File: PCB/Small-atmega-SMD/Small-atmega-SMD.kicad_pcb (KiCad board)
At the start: 2 copper layers, 65.1 x 96.9 mm, 31 parts, among them J1 Daisy port out, J2 ICSP_ISP6, J3 UART, J4 Daisy port in, K1 HYC77-TF09-200, U1 PC817C-S, U2 ATmega328P-AU, U3 SE5218, U4 TXB0104PWR, Y1 Resonator_GND2

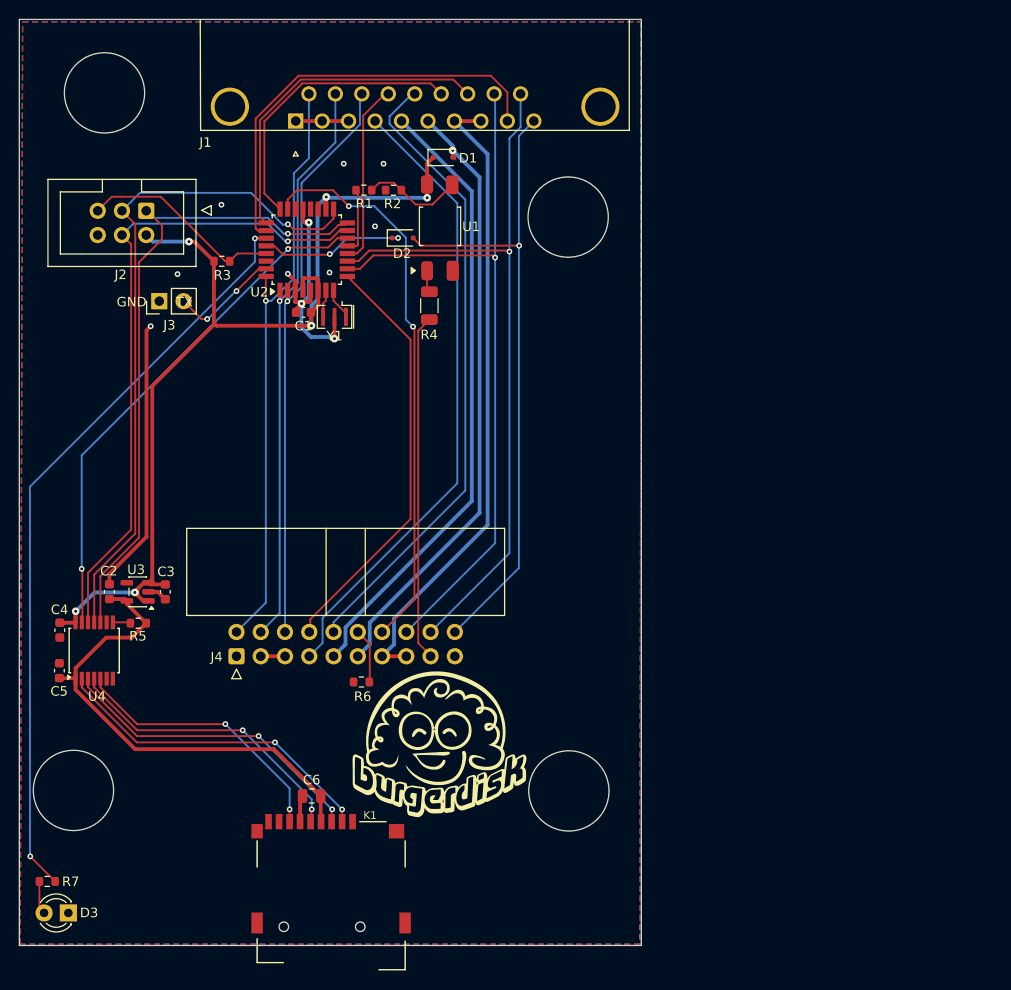
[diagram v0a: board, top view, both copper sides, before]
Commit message: Add SD module header, for hackers
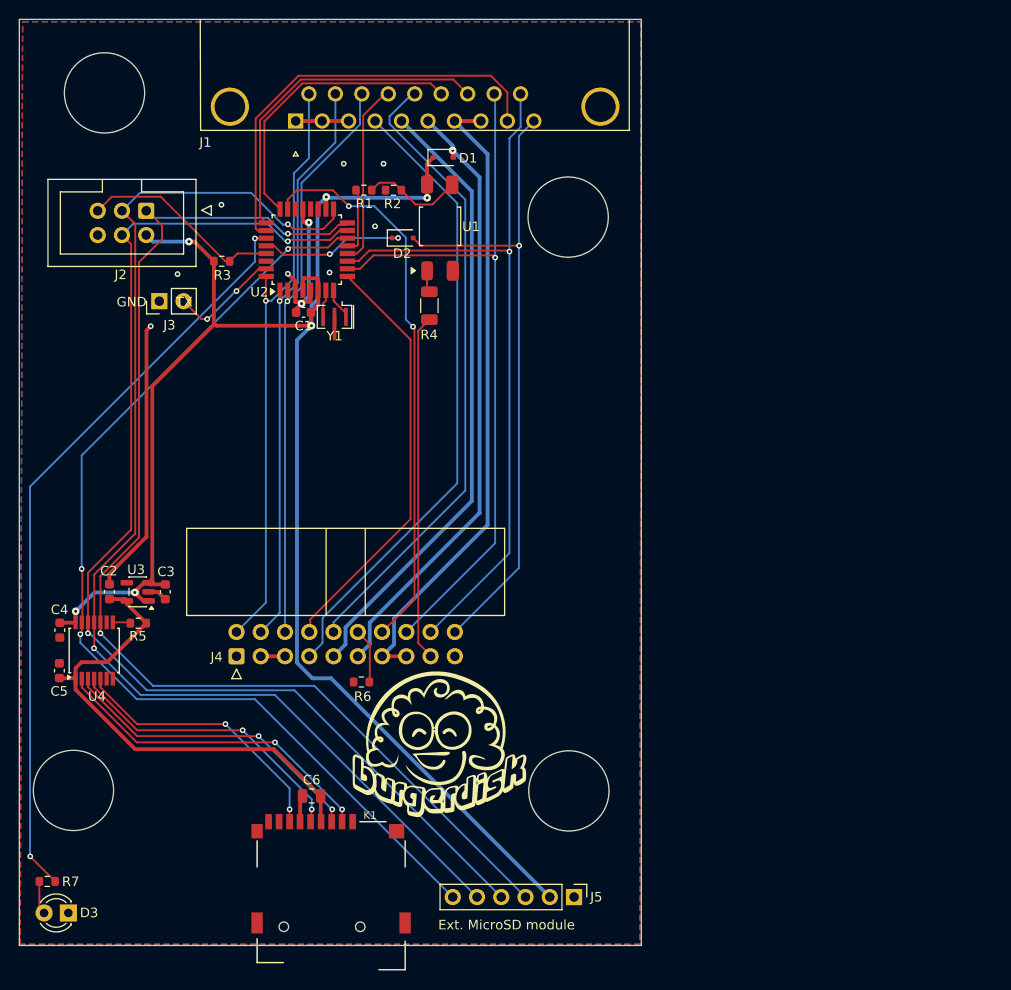
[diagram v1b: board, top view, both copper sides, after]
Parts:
- added J5: Ext. MicroSD module, Connector_PinHeader_2.54mm:PinHeader_1x06_P2.54mm_Vertical, F.Cu at (157.6, 135.2)
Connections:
- D3 pad 2: Net-(D3-A) -> LED
- R7 pad 1: Net-(D3-A) -> LED
- R7 pad 2: LED -> Net-(U2-PC4)
- U2 pad 27: LED -> Net-(U2-PC4)
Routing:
- net Net-(U2-PC4): track 0.00 -> 79.3 mm, vias 0 -> 2
- net LED: track 79.3 -> 2.81 mm, vias 2 -> 0
- net 5V_burgerDisk: track 109.5 -> 182.0 mm
- net MISO: track 68.9 -> 126.0 mm, vias 1 -> 2
- net MOSI: track 68.2 -> 124.1 mm, vias 1 -> 2
- net SCK: track 71.4 -> 125.0 mm, vias 1 -> 2
- net CS: track 54.7 -> 106.9 mm, vias 2 -> 3
- net GND: track 69.1 -> 62.7 mm, vias 11 -> 10
- net Net-(D3-A): track 2.81 -> 0.00 mm

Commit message: Add solder pads for hacking
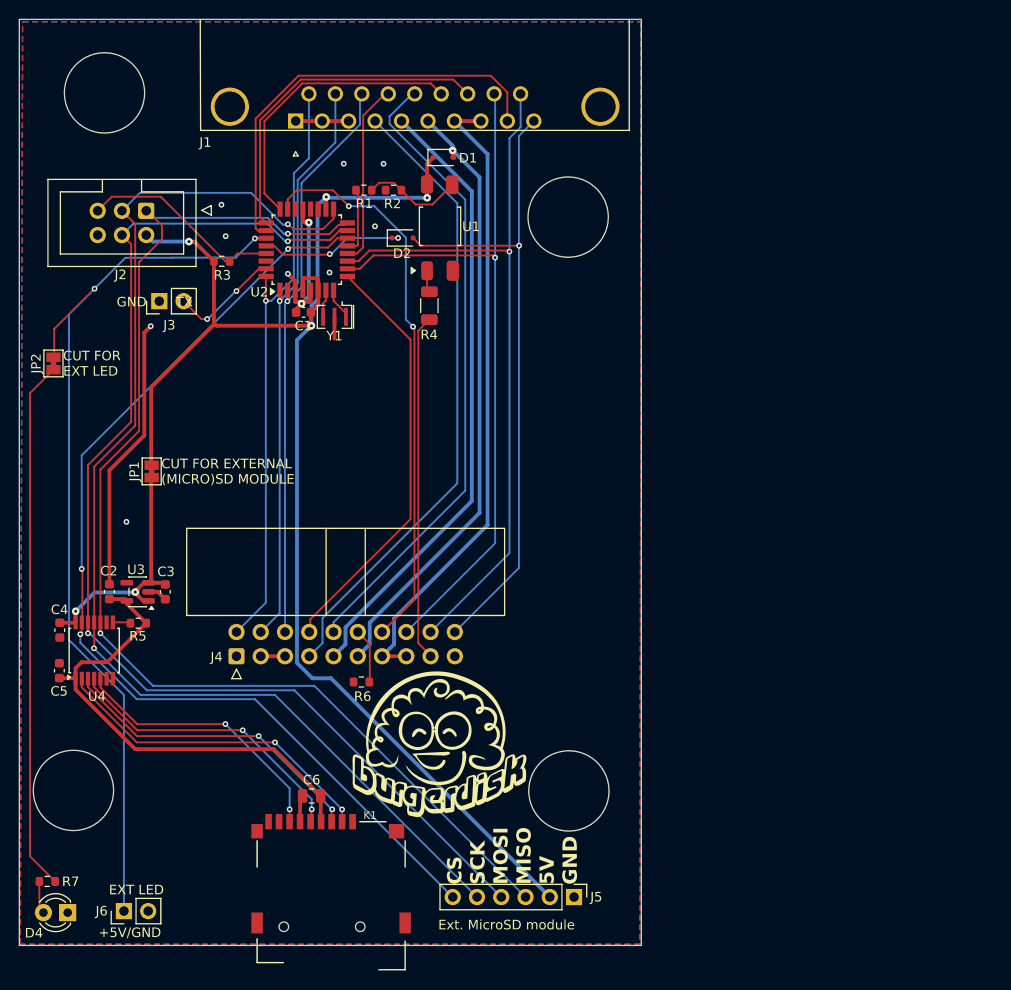
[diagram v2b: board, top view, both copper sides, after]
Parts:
- removed D3: LED, LED_THT:LED_D3.0mm
- added D4: LED, LED_THT:LED_D3.0mm, F.Cu at (104.6, 136.8)
- added J6: EXT LED, Connector_PinHeader_2.54mm:PinHeader_1x02_P2.54mm_Vertical, F.Cu at (110.5, 136.7)
- added JP1: INT MICROSD JUMPER, Jumper:SolderJumper-2_P1.3mm_Bridged_Pad1.0x1.5mm, F.Cu at (113.4, 90.6)
- added JP2: INT/EXT LED JUMPER, Jumper:SolderJumper-2_P1.3mm_Bridged_Pad1.0x1.5mm, F.Cu at (103.1, 79.3)
- C1: value 100nF -> 100n
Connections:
- C3 pad 2: 5V_burgerDisk -> 5V_intMicroSD
- C4 pad 2: 5V_burgerDisk -> 5V_intMicroSD
- R7 pad 1: LED -> Net-(D4-A)
- R7 pad 2: Net-(U2-PC4) -> Net-(JP2-A)
- U2 pad 27: Net-(U2-PC4) -> LED
- U3 pad 1: 5V_burgerDisk -> 5V_intMicroSD
- U3 pad 3: 5V_burgerDisk -> 5V_intMicroSD
- U4 pad 14: 5V_burgerDisk -> 5V_intMicroSD
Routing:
- net LED: track 2.81 -> 98.0 mm, vias 0 -> 2
- net Net-(U2-PC4): track 79.3 -> 0.00 mm, vias 2 -> 0
- net Net-(JP2-A): track 0.00 -> 55.7 mm
- net 5V_burgerDisk: track 182.0 -> 153.6 mm, vias 6 -> 4
- net 5V_intMicroSD: track 0.00 -> 27.2 mm, vias 0 -> 2
- net Net-(D4-A): track 0.00 -> 3.44 mm
- net GND: vias 10 -> 11
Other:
- board text added: "+5V/GND"
- board text added: "CS SCK MOSI MISO 5V GND"
- board text added: "CUT FOR EXT LED"
- board text added: "CUT FOR EXTERNAL (MICRO)SD MODULE"

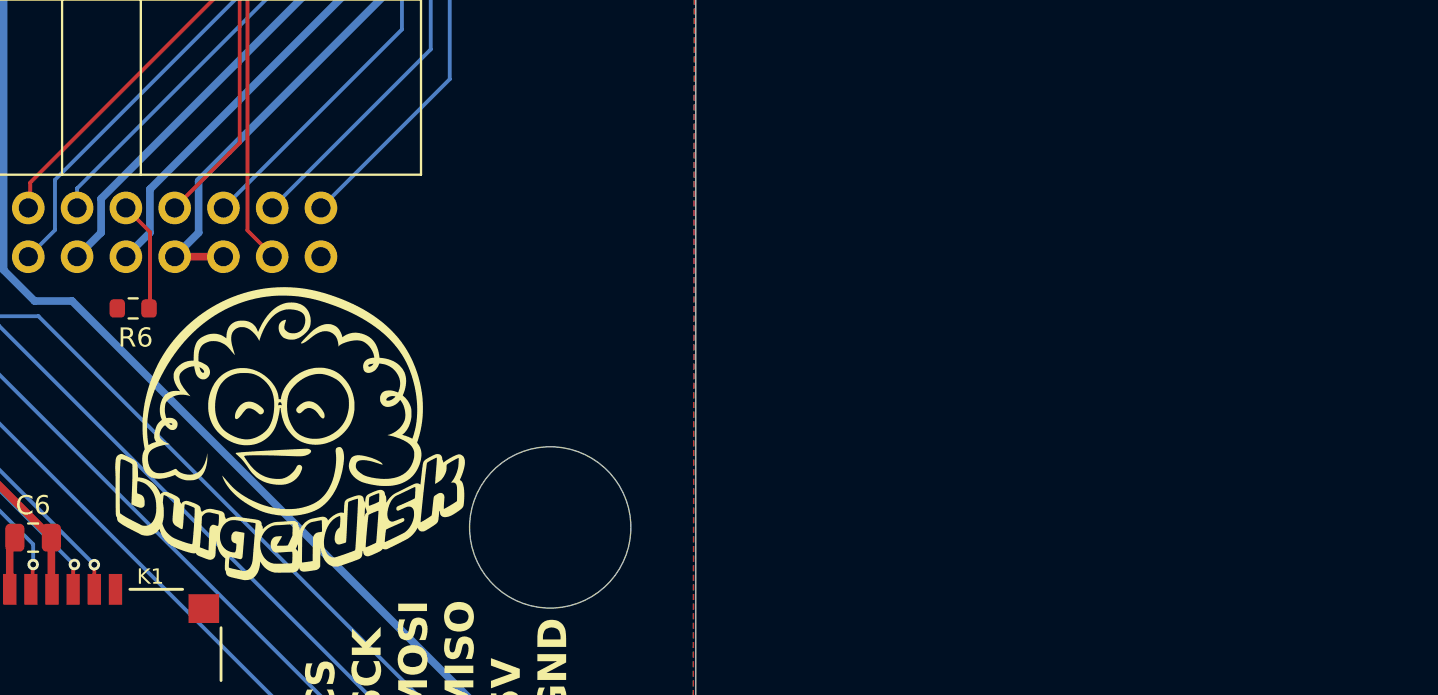
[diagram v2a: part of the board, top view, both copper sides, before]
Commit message: Move logo out of PCB
until I'm sure Rebecca's estate is OK with it
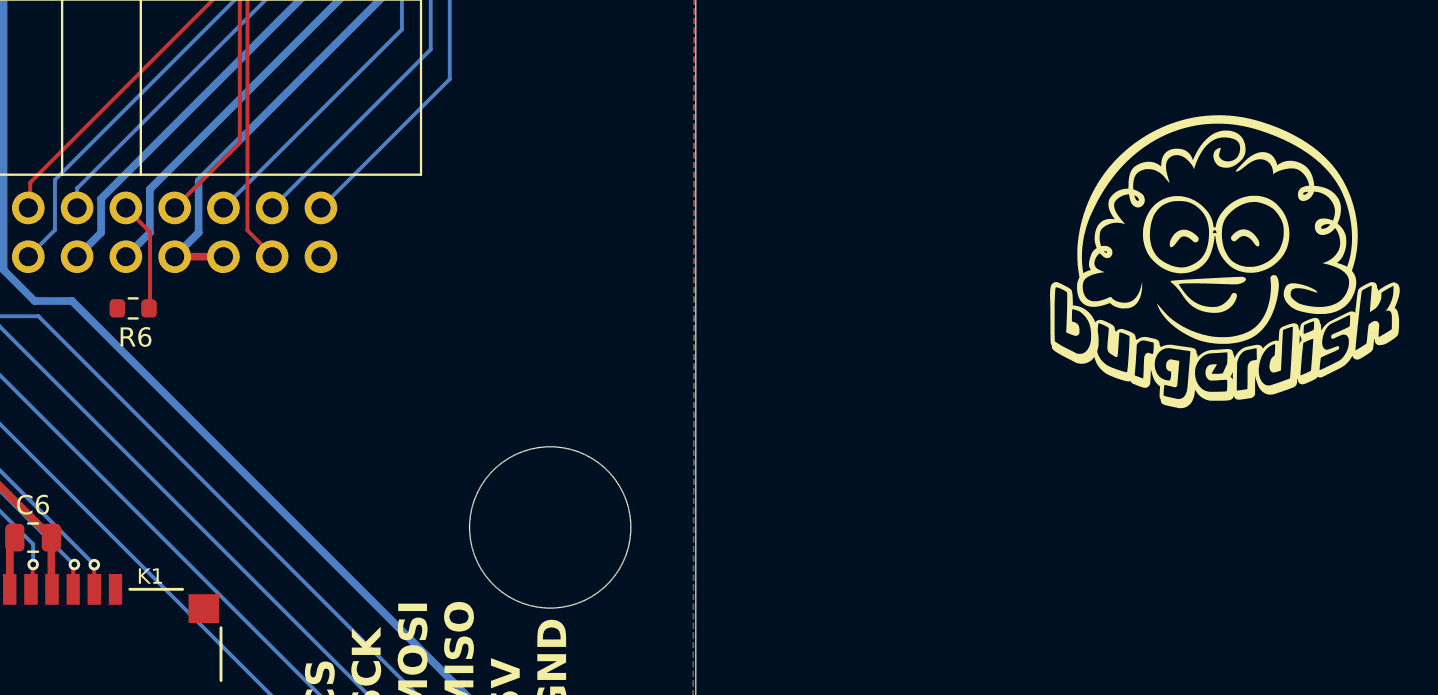
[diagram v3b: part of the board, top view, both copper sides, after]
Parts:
- moved G*** 49.5 mm to (192.2, 110.3)
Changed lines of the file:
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@@
 	(footprint "LOGO"
 		(layer "F.Cu")
-		(at 143.4846 119.253)
+		(at 192.162905 110.299597)
 		(property "Reference" "G***"
 			(at 0 0 0)

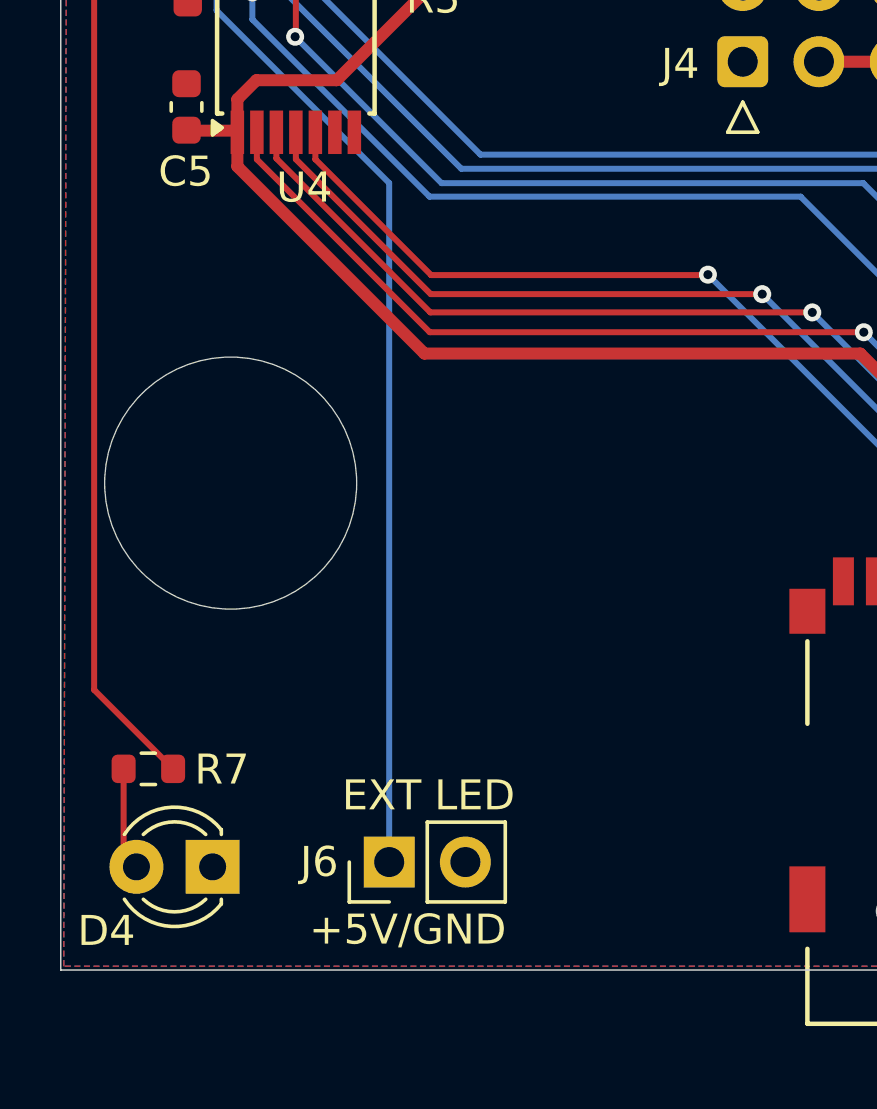
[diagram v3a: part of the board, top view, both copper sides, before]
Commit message: Switch some parts to Basic
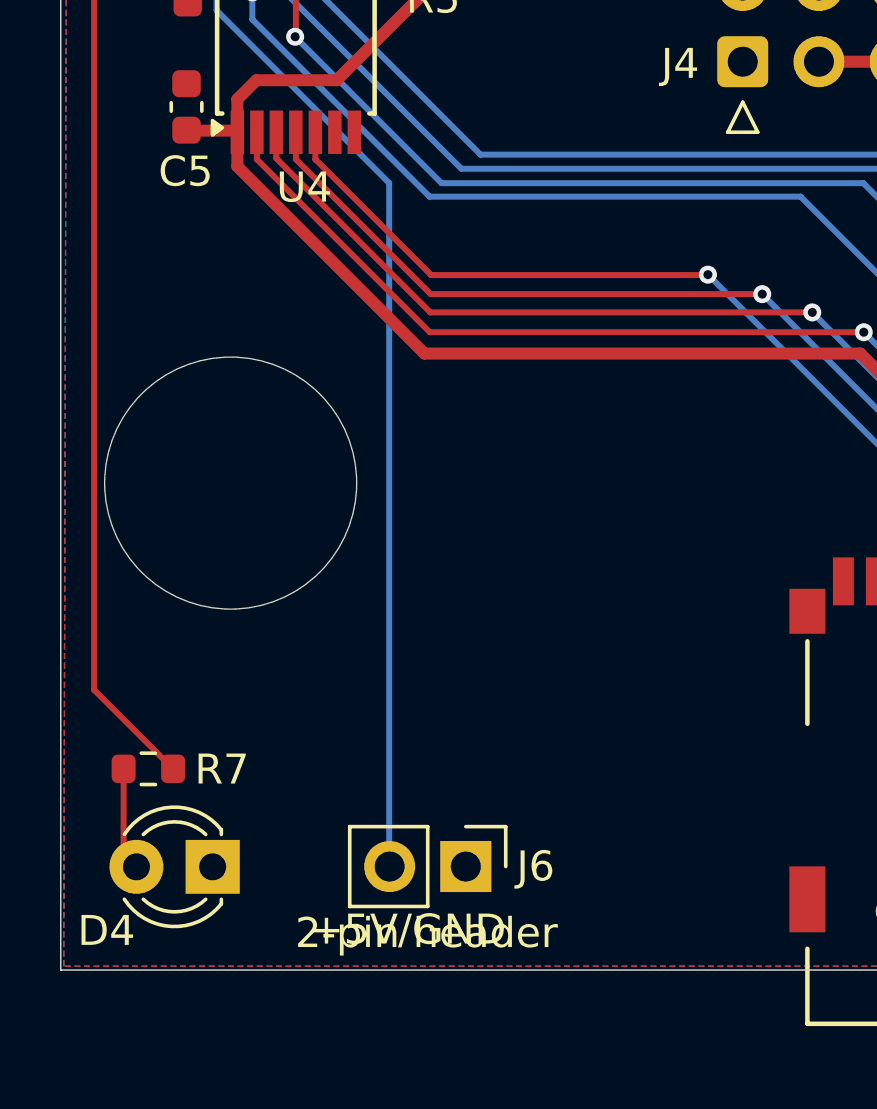
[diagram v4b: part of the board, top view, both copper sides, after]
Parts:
- J3: value UART -> 2-pin header
- J6: value EXT LED -> 2-pin header
- moved J6 2.56 mm to (113.0, 136.8), turned to -90 degrees
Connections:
- J6 pad 1: LED -> GND
- J6 pad 2: GND -> LED
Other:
- board text added: "If using an external SD or MicroSD module, cut power to the internal one by cutting the trace in the JP1 jumper. If using an external LED (with external resistor), cut power to the internal one by cutting the trace in the JP2 jumper."

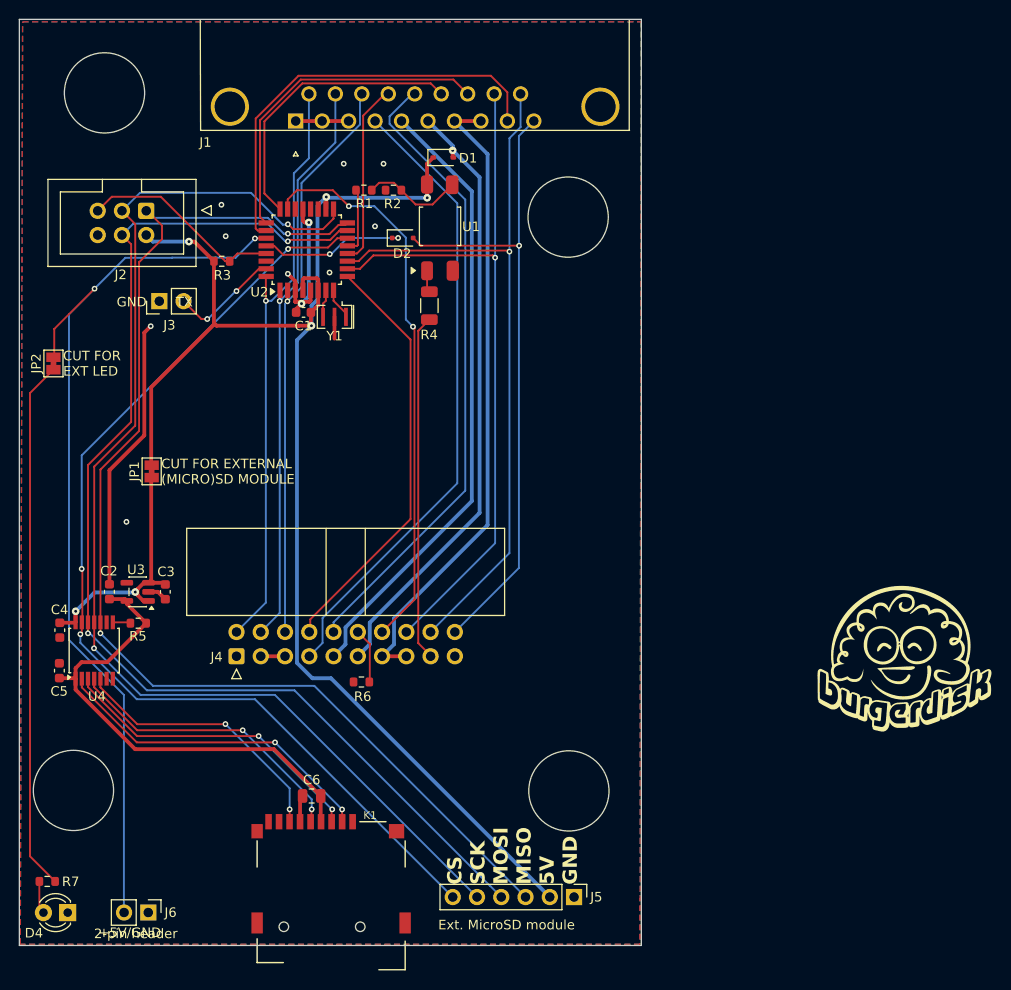
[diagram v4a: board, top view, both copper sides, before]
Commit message: Silkscreen/via avoidance
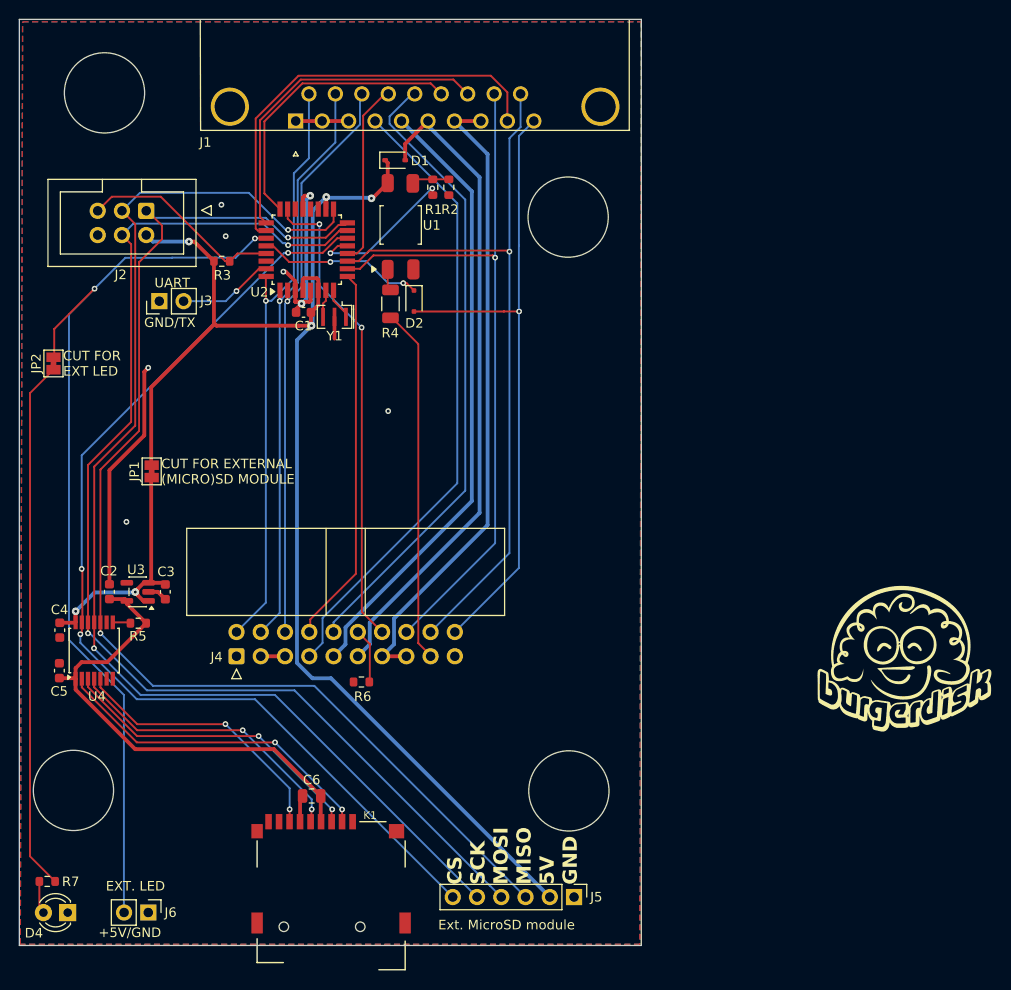
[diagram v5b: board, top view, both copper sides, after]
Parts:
- moved R1 7.22 mm to (142.8, 60.9), turned to 90 degrees
- moved D2 6.70 mm to (140.8, 72.8), turned to -90 degrees
- moved R2 5.80 mm to (144.5, 60.9), turned to 90 degrees
- moved D1 5.05 mm to (138.9, 58.0)
- moved U1 4.12 mm to (139.4, 64.8)
- moved R4 4.08 mm to (138.4, 73.1)
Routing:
- net DRV2_burgerDisk: track 6.67 -> 16.3 mm, vias 0 -> 2
- net DRV1_in: track 58.9 -> 50.0 mm
- net Net-(R1-Pad2): track 10.5 -> 3.95 mm
- net 5V_burgerDisk: track 153.6 -> 148.2 mm
- net 5V_apple2: track 64.3 -> 69.1 mm, vias 1 -> 0
- net PH3_in: track 44.2 -> 39.5 mm
- net WRPROT_in: track 15.5 -> 17.5 mm
- net TX: track 11.6 -> 10.1 mm, vias 2 -> 1
- net DRV2_in: track 36.2 -> 37.2 mm
- net GND: track 62.7 -> 61.8 mm, vias 11 -> 8
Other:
- board text added: "EXT. LED"
- board text added: "GND/TX"
- board text added: "UART"
- board text removed: "GND TX"
